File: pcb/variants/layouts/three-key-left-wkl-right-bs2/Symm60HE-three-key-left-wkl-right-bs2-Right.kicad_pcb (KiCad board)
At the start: 2 copper layers, 145.9 x 104.7 mm, 166 parts

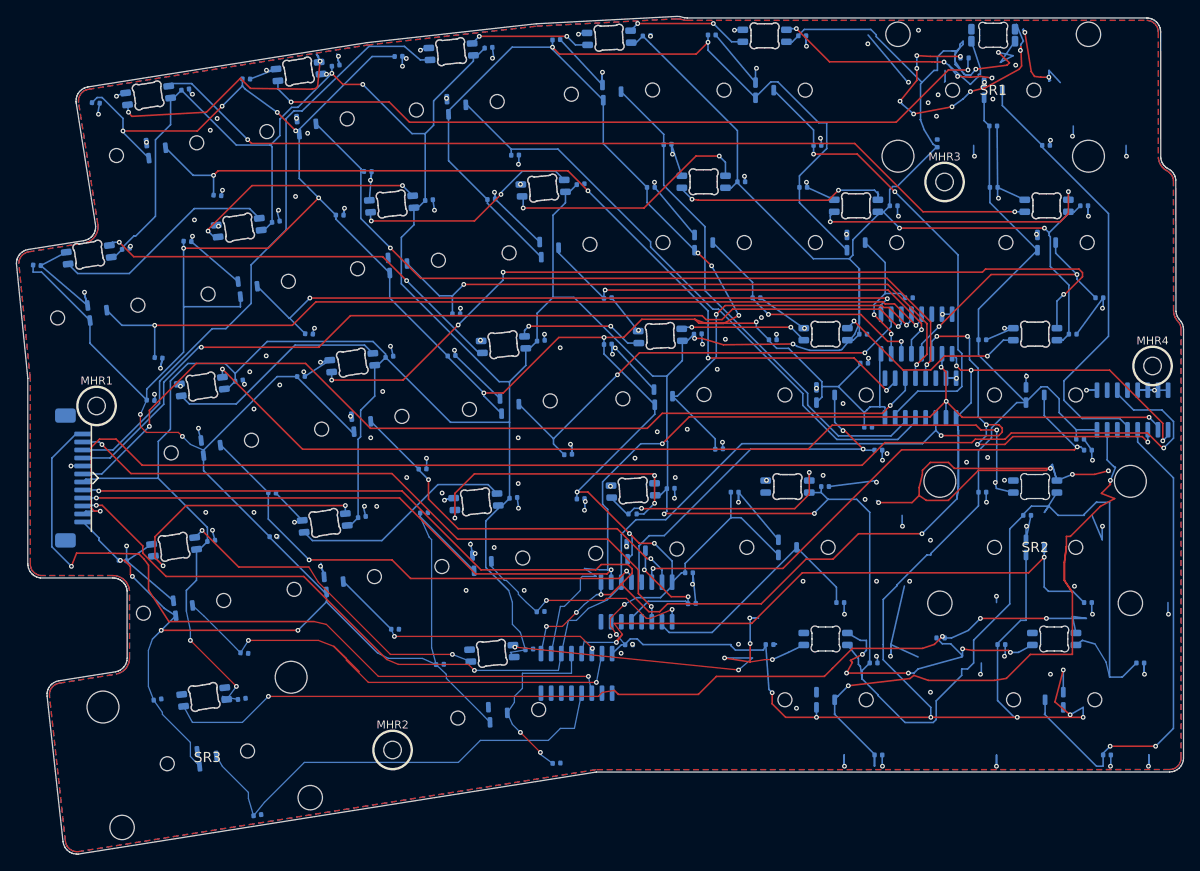
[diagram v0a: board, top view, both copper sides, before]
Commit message: Move every LED into the switch's south RGB pocket
The reverse-mount SK6812MINI-E sat 7.60 mm north of each key, shining into
the Gateron KS-20's opaque cover rather than its window. All 65 LEDs now sit
5.35 mm south of their key, in the pocket the cover is moulded for, so the
board lights like a Wooting 60HE+ backlight instead of a pass-through for a
transparent cap. Switches install with their RGB pocket toward the user; the
plate cutout and the alignment pins are symmetric, so nothing else changes.

Both halves were re-routed around the new apertures and are fully connected
with no DRC errors: 247 vias on the left (was 251) and 418 on the right (was
393). A handful of GND pads the apertures fence off on both layers reach the
plane through a via inside the pad, so the order checklist now asks for tented
vias. The pours' copies of the apertures moved with the LEDs -- they had been
left behind at the old positions, cutting some 800 mm2 of ground per layer for
openings that were no longer there.

The fixed-layout derivatives needed more than a copy of that work. Each one
restores its close-pair switches' alignment drills to the horizontal axis, and
the masters' new routing ran where those drills land, so the finishing pass
grew a repair loop: give a finding room, route it again, and keep the result
only if nothing got worse -- no new opens, and never a short. A net the router
cannot put back keeps the copper it had. Where a gap is short by microns the
trace is bent clear rather than ripped, because on a board this full a ripped
trace comes back exactly where it was. An LED only returns to its fixed-layout
row when that space is free, and the stabilisers keep the master's angle now
that they no longer have a northern aperture to face. All sixteen boards report
zero DRC and connectivity errors, and the audit checks the pocket window rather
than a nominal offset.

The panel gained the same care: a break row would have drilled through a trace
running along the right half'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
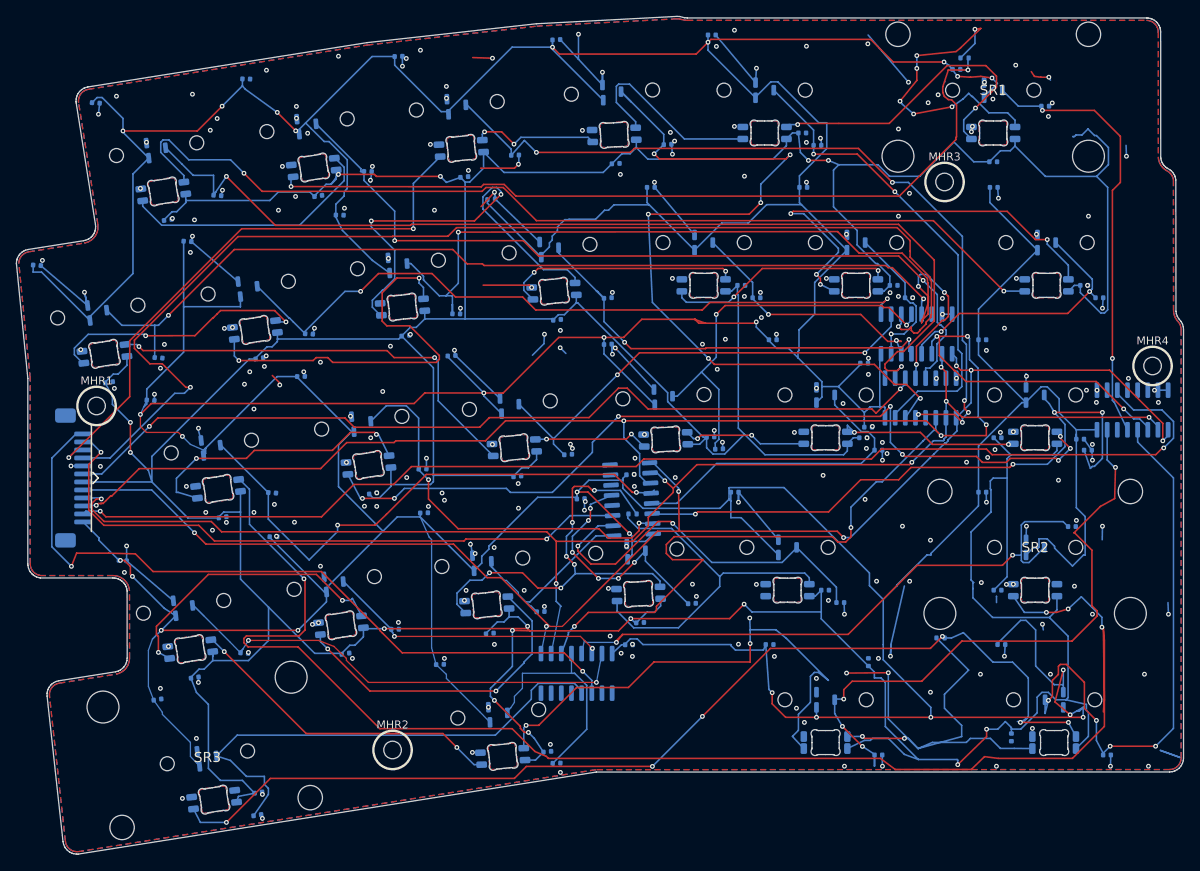
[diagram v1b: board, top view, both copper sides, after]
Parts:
- moved CRGBR31 18.6 mm to (281.4, 90.4), turned to -90 degrees
- moved CRGBR11 17.2 mm to (224.6, 38.2)
- moved CRGBR15 17.2 mm to (219.6, 57.8)
- moved CRGBR12 17.2 mm to (205.6, 40.2)
- moved CRGBR19 17.2 mm to (201.6, 59.9)
- moved CRGBR13 17.2 mm to (187.4, 43.1)
- moved CRGBR24 17.2 mm to (234.9, 76.1)
- moved CRGBR25 17.2 mm to (216.2, 77.4)
- moved CRGBR26 17.2 mm to (198.1, 80.0)
- moved CRGBR27 17.2 mm to (179.3, 83.0)
- moved CRGBR20 17.2 mm to (182.7, 62.9)
- moved CRGBR14 16.8 mm to (168.5, 46.0)
- moved CRGBR1 16.4 mm to (213.0, 20.4)
- moved CRGBR2 16.4 mm to (231.9, 18.7)
- moved CRGBR6 16.4 mm to (194.7, 22.7)
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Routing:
- net GND: track 359.0 -> 202.7 mm, vias 175 -> 260
- net +3V3A: track 883.4 -> 1001.0 mm, vias 32 -> 26
- net RGB_R_20: track 113.2 -> 185.1 mm, vias 3 -> 4
- net MUX_A0: track 191.8 -> 254.2 mm, vias 8 -> 9
- net RGB_R_21: track 55.7 -> 0.00 mm, vias 4 -> 0
- net HE_R02: track 63.9 -> 105.1 mm, vias 0 -> 6
- net ADC_R2: track 114.2 -> 148.9 mm
- net HE_R08: track 78.9 -> 110.5 mm, vias 2 -> 4
- net HE_R01: track 77.0 -> 102.4 mm, vias 0 -> 6
- net RGB_R_29: track 37.5 -> 62.8 mm, vias 5 -> 4
- net RGB_R_11: track 28.4 -> 52.9 mm
- net RGB_R_08: track 35.4 -> 55.2 mm, vias 2 -> 4
- net RGB_R_12: track 30.1 -> 49.7 mm
- net MUX_A2: track 203.0 -> 184.1 mm, vias 8 -> 7
- net HE_R23: track 31.1 -> 48.2 mm, vias 0 -> 2
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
